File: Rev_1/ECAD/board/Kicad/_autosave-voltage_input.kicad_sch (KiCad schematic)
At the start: 21 parts, among them Q1 PMOS, Q2 PNP, Q3 PNP

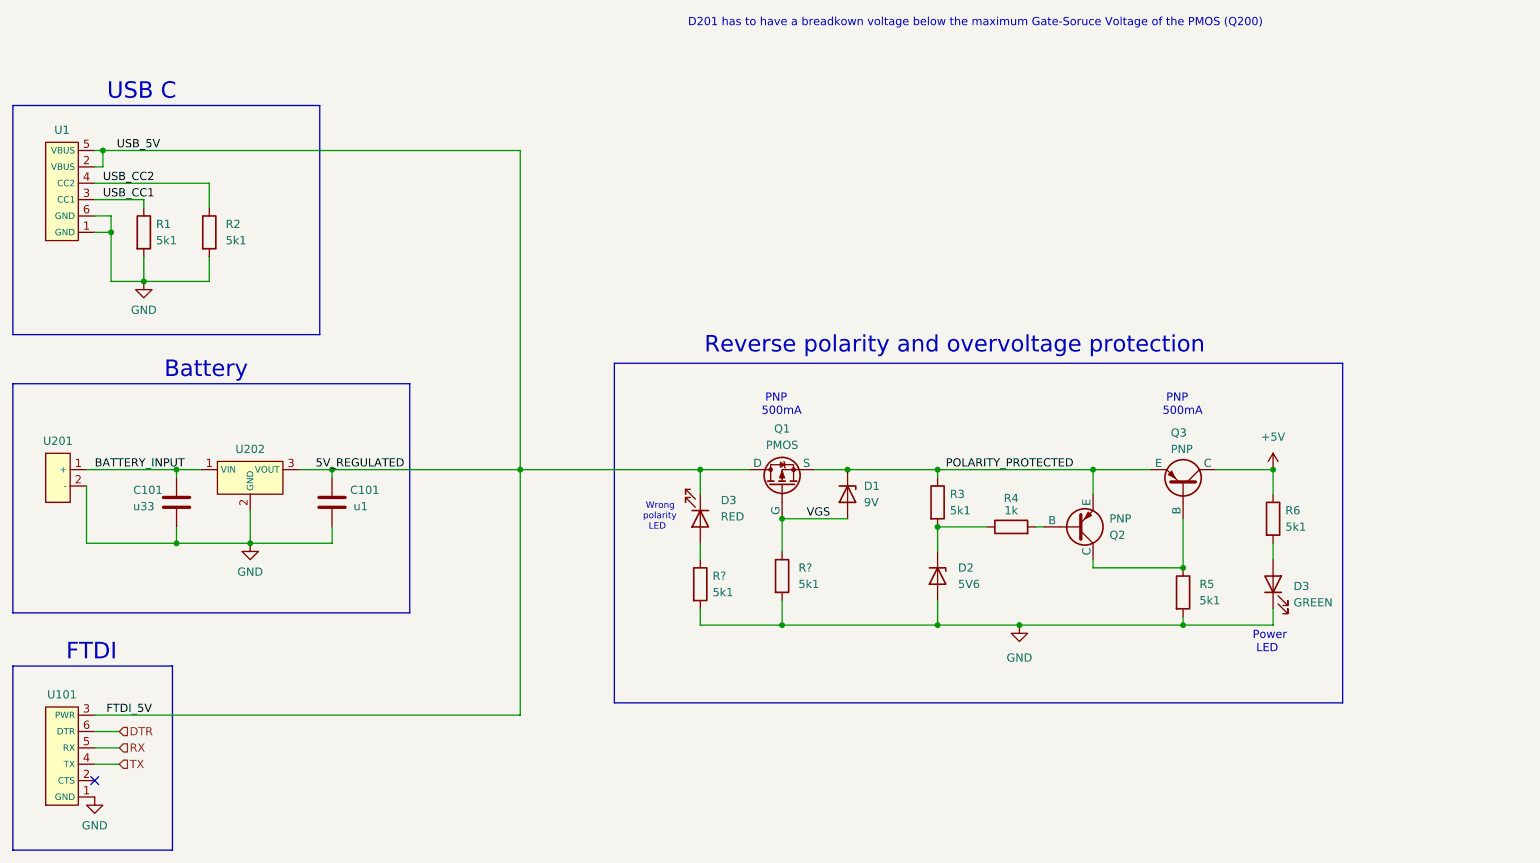
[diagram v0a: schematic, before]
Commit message: Updated Symbol library´and added SD Card Reader to schematic
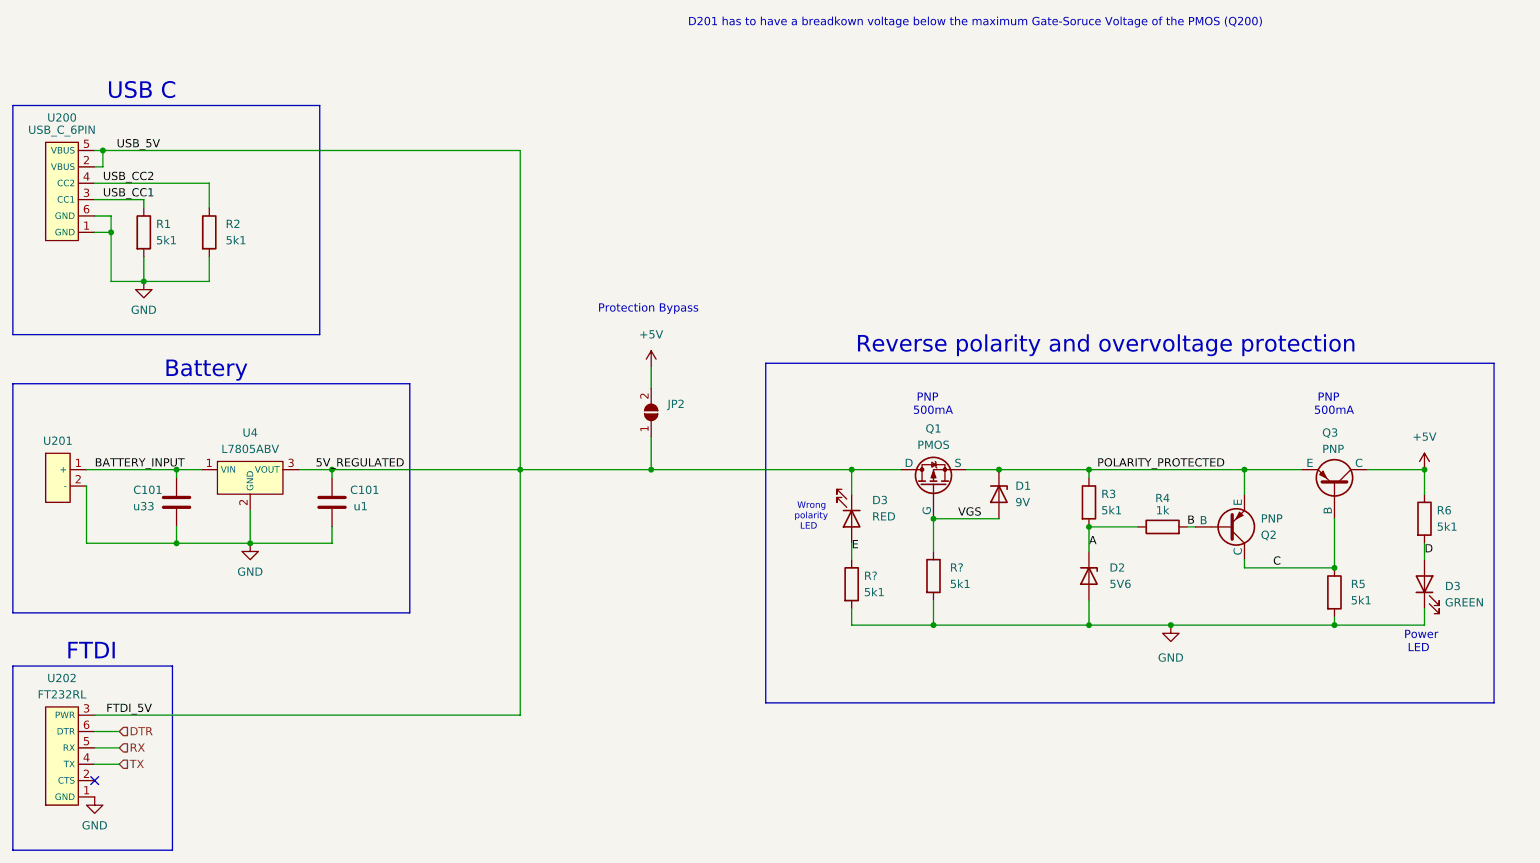
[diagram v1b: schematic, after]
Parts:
- removed U1: ~, symbol EEPROM_PROGRAMMER:USB_C_6PIN
- removed U101: ~, symbol EEPROM_PROGRAMMER:FT232RL
- removed U202: ~, symbol EEPROM_PROGRAMMER:L7805ABV
- added JP2: SolderJumper_2_Open, Jumper:SolderJumper-3_P1.3mm_Open_Pad1.0x1.5mm, symbol Jumper:SolderJumper_2_Open
- added U200: USB_C_6PIN, symbol EEPROM_PROGRAMMER:USB_C_6PIN
- added U202: FT232RL, symbol EEPROM_PROGRAMMER:FT232RL
- added U4: L7805ABV, symbol EEPROM_PROGRAMMER:L7805ABV
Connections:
- net +5V: now also JP2.2 (B)
- net 5V_REGULATED: now also JP2.1 (A), U200.2 (VBUS), U200.5 (VBUS), U202.3 (PWR), U4.3 (VOUT)
- net BATTERY_INPUT: now also U4.1 (VIN)
- net DTR: now also U202.6 (DTR)
- net GND: now also U200.1 (GND), U200.6 (GND), U202.1 (GND), U4.2 (GND)
- net RX: now also U202.5 (RX)
- net TX: now also U202.4 (TX)
- net USB_CC1: now also U200.3 (CC1)
- net USB_CC2: now also U200.4 (CC2)
- net E: now reaches D3.2 (A), R?.1
- net C: now reaches Q2.1 (C), Q3.2 (B), R5.1
- net D: now reaches D3.2 (A), R6.2
- net A: now reaches D2.1 (K), R3.2, R4.1
- net B: now reaches Q2.2 (B), R4.2
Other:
- note added: "Protection Bypass"
- moved on the sheet: D1, D2, D3, Q1, Q2, Q3, R3, R4, R5, R6, R?
